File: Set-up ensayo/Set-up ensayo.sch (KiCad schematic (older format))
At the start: 0 parts

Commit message: Terminé con el paso 1 de proceso y comencé con el paso 2 colocando componentes, falta el interruptor para cambiar de estado del PCB (ensayo/configuración)
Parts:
- added H? (x4): MountingHole_Pad, symbol Mechanical:MountingHole_Pad
- added J?: Conn_Coaxial, symbol Connector:Conn_Coaxial
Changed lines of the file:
@@
 EESchema Schematic File Version 4
+LIBS:Set-up ensayo-cache
 EELAYER 29 0
 EELAYER END
@@
 Comment4 ""
 $EndDescr
+$Comp
+L Mechanical:MountingHole_Pad H?
+U 1 1 5D42DD18
+P 2650 2850
+F 0 "H?" H 2750 2899 50  0000 L CNN
+F 1 "MountingHole_Pad" H 2750 2808 50  0000 L CNN
+F 2 "" H 2650 2850 50  0001 C CNN
+F 3 "~" H 2650 2850 50  0001 C CNN
+	1    2650 2850
+	1    0    0    -1
+$EndComp
+$Comp
+L Mechanical:MountingHole_Pad H?
+U 1 1 5D42E2DA
+P 5150 2850
+F 0 "H?" H 5250 2899 50  0000 L CNN
+F 1 "MountingHole_Pad" H 5250 2808 50  0000 L CNN
+F 2 "" H 5150 2850 50  0001 C CNN
+F 3 "~" H 5150 2850 50  0001 C CNN
+	1    5150 2850
+	1    0    0    -1
+$EndComp
+$Comp
+L Mechanical:MountingHole_Pad H?
+U 1 1 5D42E927
+P 2650 5000
+F 0 "H?" H 2750 5049 50  0000 L CNN
+F 1 "MountingHole_Pad" H 2750 4958 50  0000 L CNN
+F 2 "" H 2650 5000 50  0001 C CNN
+F 3 "~" H 2650 5000 50  0001 C CNN
+	1    2650 5000
+	1    0    0    -1
+$EndComp
+$Comp
+L Mechanical:MountingHole_Pad H?
+U 1 1 5D42EA1B
+P 5200 5100
+F 0 "H?" H 5300 5149 50  0000 L CNN
+F 1 "MountingHole_Pad" H 5300 5058 50  0000 L CNN
+F 2 "" H 5200 5100 50  0001 C CNN
+F 3 "~" H 5200 5100 50  0001 C CNN
+	1    5200 5100
+	1    0    0    -1
+$EndComp
+$Comp
+L Connector:Conn_Coaxial J?
+U 1 1 5D42F04D
+P 3200 3800
+F 0 "J?" H 3300 3775 50  0000 L CNN
+F 1 "Conn_Coaxial" H 3300 3684 50  0000 L CNN
+F 2 "" H 3200 3800 50  0001 C CNN
+F 3 " ~" H 3200 3800 50  0001 C CNN
+	1    3200 3800
+	1    0    0    -1
+$EndComp
 $EndSCHEMATC

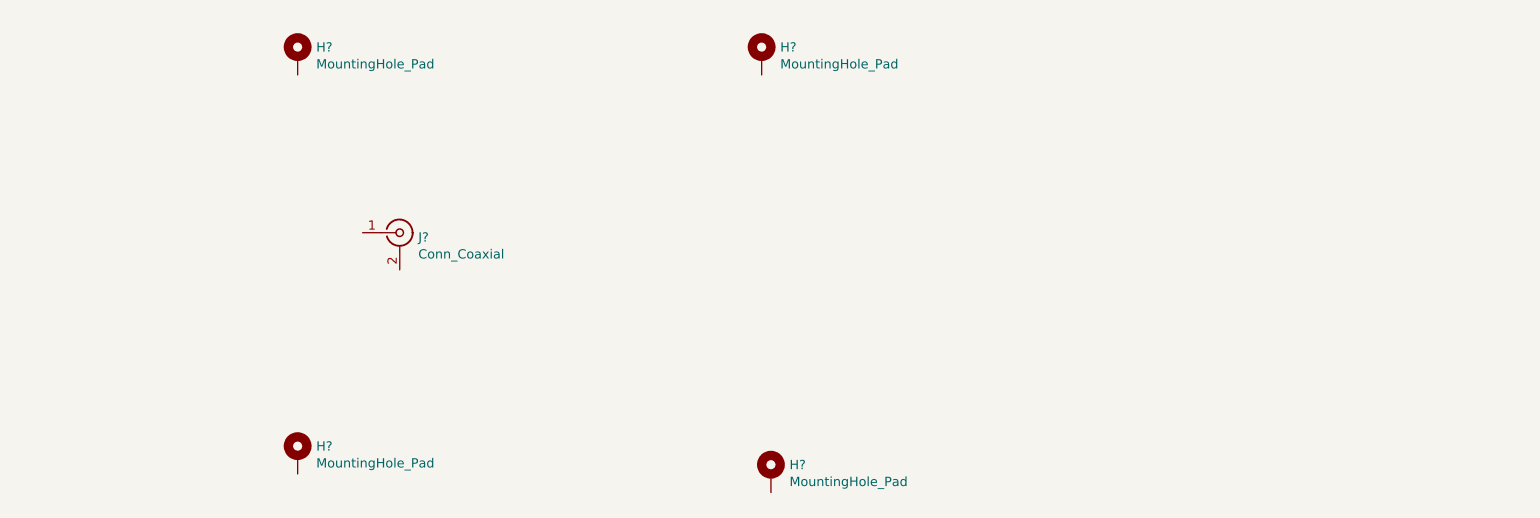
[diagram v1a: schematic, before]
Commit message: Cree componente circuit breaker en librería nueva Simbolo-ensayo y comencé a colocar los símbolos de los componentes
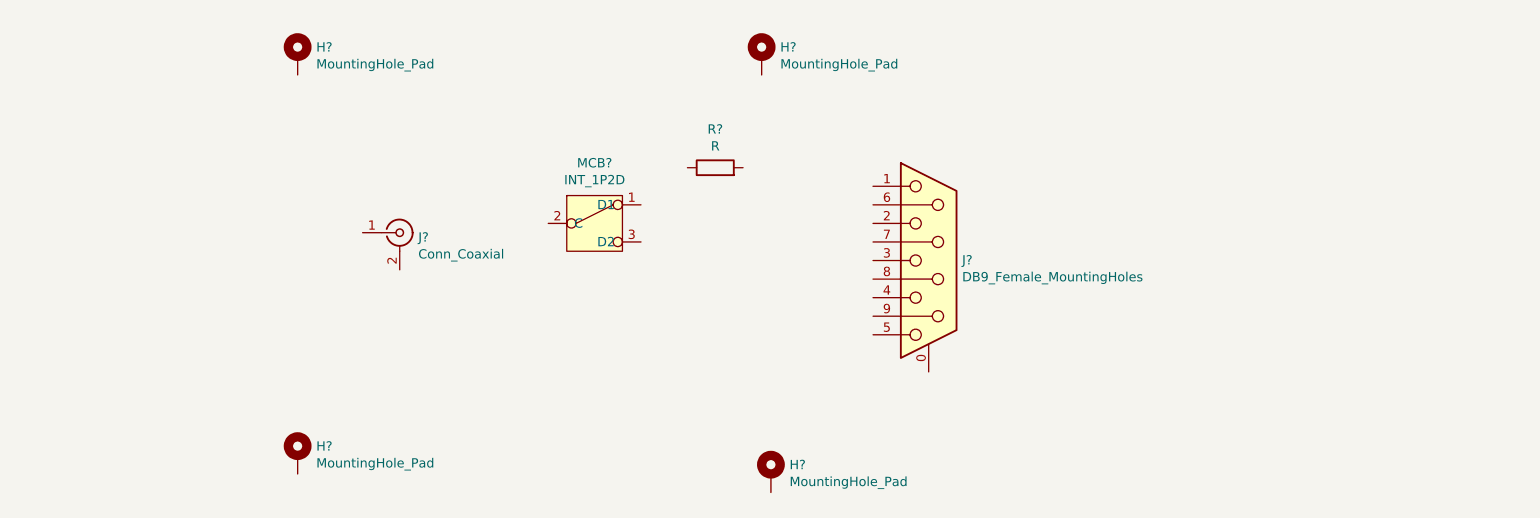
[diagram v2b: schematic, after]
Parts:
- added J?: DB9_Female_MountingHoles, symbol Connector:DB9_Female_MountingHoles
- added MCB?: INT_1P2D, symbol Simbolo-ensayo:INT_1P2D
- added R?: R, symbol Device:R
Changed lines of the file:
@@
+	1    0    0    -1
+$EndComp
+$Comp
+L Simbolo-ensayo:INT_1P2D MCB?
+U 1 1 5D440928
+P 4250 3750
+F 0 "MCB?" H 4250 4075 50  0000 C CNN
+F 1 "INT_1P2D" H 4250 3984 50  0000 C CNN
+F 2 "" H 4250 3750 50  0001 C CNN
+F 3 "" H 4250 3750 50  0001 C CNN
+	1    4250 3750
+	1    0    0    -1
+$EndComp
+$Comp
+L Device:R R?
+U 1 1 5D441970
+P 4900 3450
+F 0 "R?" V 5107 3450 50  0000 C CNN
+F 1 "R" V 5016 3450 50  0000 C CNN
+F 2 "" V 4830 3450 50  0001 C CNN
+F 3 "~" H 4900 3450 50  0001 C CNN
+	1    4900 3450
+	0    -1   -1   0
+$EndComp
+$Comp
+L Connector:DB9_Female_MountingHoles J?
+U 1 1 5D442DB3
+P 6050 3950
+F 0 "J?" H 6230 3952 50  0000 L CNN
+F 1 "DB9_Female_MountingHoles" H 6230 3861 50  0000 L CNN
+F 2 "" H 6050 3950 50  0001 C CNN
+F 3 " ~" H 6050 3950 50  0001 C CNN
+	1    6050 3950
 	1    0    0    -1
 $EndComp

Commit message: Agregué puntos de pruebas y campo de función en cada componente del esquema, fin de segundo paso en proceso
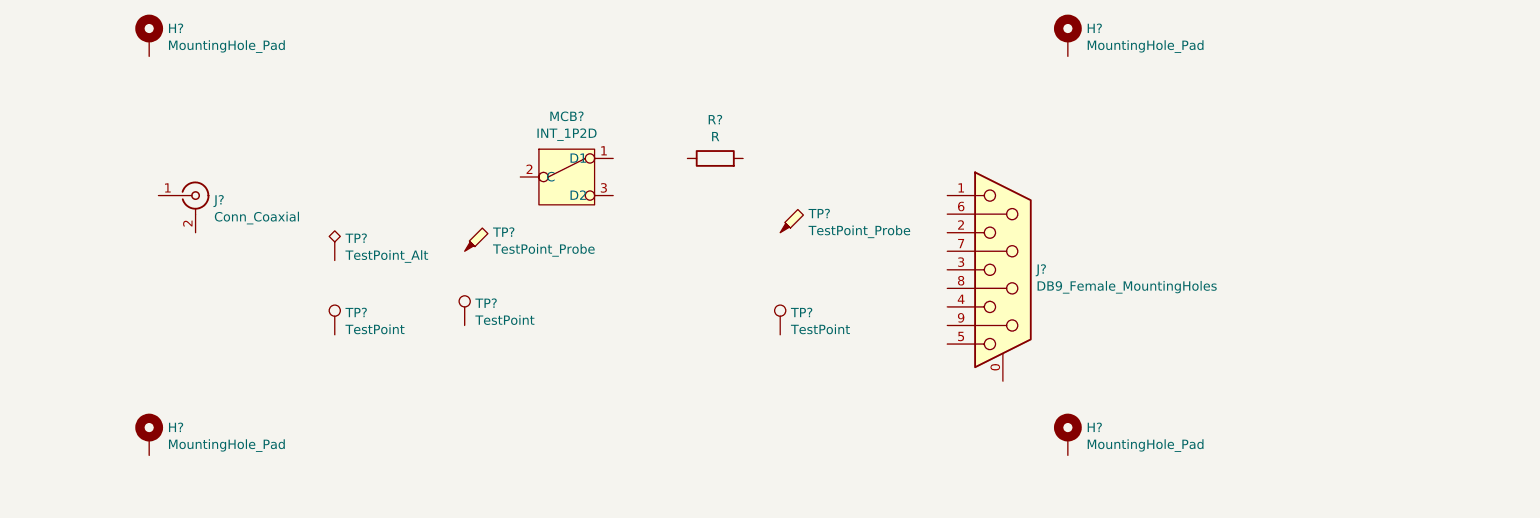
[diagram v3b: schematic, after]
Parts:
- added TP? (x2): TestPoint_Probe, symbol Connector:TestPoint_Probe
- added TP? (x3): TestPoint, symbol Connector:TestPoint
- added TP?: TestPoint_Alt, symbol Connector:TestPoint_Alt
- H? (x4): Función (none) -> Fijación e interfaz eléctrica con chasis
- J?: Función (none) -> Interfaz eléctrica con generador de señales
- J?: Función (none) -> Interfaz eléctrica con sensores
- MCB?: Función (none) -> Interruptor HMI para cambio enter ajuste y ensayo
- R?: Función (none) -> Resistencia de medición de sensor
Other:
- moved on the sheet: H?, J?, MCB?, R?
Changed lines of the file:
@@
 L Mechanical:MountingHole_Pad H?
 U 1 1 5D42DD18
-P 2650 2850
-F 0 "H?" H 2750 2899 50  0000 L CNN
-F 1 "MountingHole_Pad" H 2750 2808 50  0000 L CNN
-F 2 "" H 2650 2850 50  0001 C CNN
-F 3 "~" H 2650 2850 50  0001 C CNN
-	1    2650 2850
+P 1850 2750
+F 0 "H?" H 1950 2799 50  0000 L CNN
+F 1 "MountingHole_Pad" H 1950 2708 50  0000 L CNN
+F 2 "" H 1850 2750 50  0001 C CNN
+F 3 "~" H 1850 2750 50  0001 C CNN
+F 4 "Fijación e interfaz eléctrica con chasis" H 1850 2750 50  0001 C CNN "Función"
+	1    1850 2750
 	1    0    0    -1
 $EndComp
@@
 L Mechanical:MountingHole_Pad H?
 U 1 1 5D42E2DA
-P 5150 2850
-F 0 "H?" H 5250 2899 50  0000 L CNN
-F 1 "MountingHole_Pad" H 5250 2808 50  0000 L CNN
-F 2 "" H 5150 2850 50  0001 C CNN
-F 3 "~" H 5150 2850 50  0001 C CNN
-	1    5150 2850
+P 6800 2750
+F 0 "H?" H 6900 2799 50  0000 L CNN
+F 1 "MountingHole_Pad" H 6900 2708 50  0000 L CNN
+F 2 "" H 6800 2750 50  0001 C CNN
+F 3 "~" H 6800 2750 50  0001 C CNN
+F 4 "Fijación e interfaz eléctrica con chasis" H 6800 2750 50  0001 C CNN "Función"
+	1    6800 2750
 	1    0    0    -1
 $EndComp
@@
 L Mechanical:MountingHole_Pad H?
 U 1 1 5D42E927
-P 2650 5000
-F 0 "H?" H 2750 5049 50  0000 L CNN
-F 1 "MountingHole_Pad" H 2750 4958 50  0000 L CNN
-F 2 "" H 2650 5000 50  0001 C CNN
-F 3 "~" H 2650 5000 50  0001 C CNN
-	1    2650 5000
+P 1850 4900
+F 0 "H?" H 1950 4949 50  0000 L CNN
+F 1 "MountingHole_Pad" H 1950 4858 50  0000 L CNN
+F 2 "" H 1850 4900 50  0001 C CNN
+F 3 "~" H 1850 4900 50  0001 C CNN
+F 4 "Fijación e interfaz eléctrica con chasis" H 1850 4900 50  0001 C CNN "Función"
+	1    1850 4900
 	1    0    0    -1
 $EndComp
@@
 L Mechanical:MountingHole_Pad H?
 U 1 1 5D42EA1B
-P 5200 5100
-F 0 "H?" H 5300 5149 50  0000 L CNN
-F 1 "MountingHole_Pad" H 5300 5058 50  0000 L CNN
-F 2 "" H 5200 5100 50  0001 C CNN
-F 3 "~" H 5200 5100 50  0001 C CNN
-	1    5200 5100
+P 6800 4900
+F 0 "H?" H 6900 4949 50  0000 L CNN
+F 1 "MountingHole_Pad" H 6900 4858 50  0000 L CNN
+F 2 "" H 6800 4900 50  0001 C CNN
+F 3 "~" H 6800 4900 50  0001 C CNN
+F 4 "Fijación e interfaz eléctrica con chasis" H 6800 4900 50  0001 C CNN "Función"
+	1    6800 4900
 	1    0    0    -1
 $EndComp
@@
 L Connector:Conn_Coaxial J?
 U 1 1 5D42F04D
-P 3200 3800
-F 0 "J?" H 3300 3775 50  0000 L CNN
-F 1 "Conn_Coaxial" H 3300 3684 50  0000 L CNN
-F 2 "" H 3200 3800 50  0001 C CNN
-F 3 " ~" H 3200 3800 50  0001 C CNN
-	1    3200 3800
+P 2100 3600
+F 0 "J?" H 2200 3575 50  0000 L CNN
+F 1 "Conn_Coaxial" H 2200 3484 50  0000 L CNN
+F 2 "" H 2100 3600 50  0001 C CNN
+F 3 " ~" H 2100 3600 50  0001 C CNN
+F 4 "Interfaz eléctrica con generador de señales" H 2100 3600 50  0001 C CNN "Función"
+	1    2100 3600
 	1    0    0    -1
 $EndComp
@@
 L Simbolo-ensayo:INT_1P2D MCB?
 U 1 1 5D440928
-P 4250 3750
-F 0 "MCB?" H 4250 4075 50  0000 C CNN
-F 1 "INT_1P2D" H 4250 3984 50  0000 C CNN
-F 2 "" H 4250 3750 50  0001 C CNN
-F 3 "" H 4250 3750 50  0001 C CNN
-	1    4250 3750
+P 4100 3500
+F 0 "MCB?" H 4100 3825 50  0000 C CNN
+F 1 "INT_1P2D" H 4100 3734 50  0000 C CNN
+F 2 "" H 4100 3500 50  0001 C CNN
+F 3 "" H 4100 3500 50  0001 C CNN
+F 4 "Interruptor HMI para cambio enter ajuste y ensayo" H 4100 3500 50  0001 C CNN "Función"
+	1    4100 3500
 	1    0    0    -1
 $EndComp
@@
 L Device:R R?
 U 1 1 5D441970
-P 4900 3450
-F 0 "R?" V 5107 3450 50  0000 C CNN
-F 1 "R" V 5016 3450 50  0000 C CNN
-F 2 "" V 4830 3450 50  0001 C CNN
-F 3 "~" H 4900 3450 50  0001 C CNN
-	1    4900 3450
+P 4900 3400
+F 0 "R?" V 5107 3400 50  0000 C CNN
+F 1 "R" V 5016 3400 50  0000 C CNN
+F 2 "" V 4830 3400 50  0001 C CNN
+F 3 "~" H 4900 3400 50  0001 C CNN
+F 4 "Resistencia de medición de sensor" V 4900 3400 50  0001 C CNN "Función"
+	1    4900 3400
 	0    -1   -1   0
 $EndComp
@@
 L Connector:DB9_Female_MountingHoles J?
 U 1 1 5D442DB3
-P 6050 3950
-F 0 "J?" H 6230 3952 50  0000 L CNN
-F 1 "DB9_Female_MountingHoles" H 6230 3861 50  0000 L CNN
-F 2 "" H 6050 3950 50  0001 C CNN
-F 3 " ~" H 6050 3950 50  0001 C CNN
-	1    6050 3950
+P 6450 4000
+F 0 "J?" H 6630 4002 50  0000 L CNN
+F 1 "DB9_Female_MountingHoles" H 6630 3911 50  0000 L CNN
+F 2 "" H 6450 4000 50  0001 C CNN
+F 3 " ~" H 6450 4000 50  0001 C CNN
+F 4 "Interfaz eléctrica con sensores" H 6450 4000 50  0001 C CNN "Función"
+	1    6450 4000
 	1    0    0    -1
 $EndComp
+$Comp
+L Connector:TestPoint_Probe TP?
+U 1 1 5D483898
+P 3550 3900
+F 0 "TP?" H 3703 4001 50  0000 L CNN
+F 1 "TestPoint_Probe" H 3703 3910 50  0000 L CNN
+F 2 "" H 3750 3900 50  0001 C CNN
+F 3 "~" H 3750 3900 50  0001 C CNN
+F 4 "Interfaz eléctrica con punta de medición V1 osciloscopio" H 3550 3900 50  0001 C CNN "Función"
+	1    3550 3900
+	1    0    0    -1
+$EndComp
+$Comp
+L Connector:TestPoint_Probe TP?
+U 1 1 5D484196
+P 5250 3800
+F 0 "TP?" H 5403 3901 50  0000 L CNN
+F 1 "TestPoint_Probe" H 5403 3810 50  0000 L CNN
+F 2 "" H 5450 3800 50  0001 C CNN
+F 3 "~" H 5450 3800 50  0001 C CNN
+F 4 "Interfaz eléctrica con punta de medición V2 osciloscopio" H 5250 3800 50  0001 C CNN "Función"
+	1    5250 3800
+	1    0    0    -1
+$EndComp
+$Comp
+L Connector:TestPoint TP?
+U 1 1 5D4852D2
+P 5250 4350
+F 0 "TP?" H 5308 4468 50  0000 L CNN
+F 1 "TestPoint" H 5308 4377 50  0000 L CNN
+F 2 "" H 5450 4350 50  0001 C CNN
+F 3 "~" H 5450 4350 50  0001 C CNN
+F 4 "Interfaz eléctrica con GND de V2 osciloscopio" H 5250 4350 50  0001 C CNN "Función"
+	1    5250 4350
+	1    0    0    -1
+$EndComp
+$Comp
+L Connector:TestPoint TP?
+U 1 1 5D4861BC
+P 3550 4300
+F 0 "TP?" H 3608 4418 50  0000 L CNN
+F 1 "TestPoint" H 3608 4327 50  0000 L CNN
+F 2 "" H 3750 4300 50  0001 C CNN
+F 3 "~" H 3750 4300 50  0001 C CNN
+F 4 "Interfaz eléctrica con GND de V1 osciloscopio" H 3550 4300 50  0001 C CNN "Función"
+	1    3550 4300
+	1    0    0    -1
+$EndComp
+$Comp
+L Connector:TestPoint_Alt TP?
+U 1 1 5D486AED
+P 2850 3950
+F 0 "TP?" H 2908 4068 50  0000 L CNN
+F 1 "TestPoint_Alt" H 2908 3977 50  0000 L CNN
+F 2 "" H 3050 3950 50  0001 C CNN
+F 3 "~" H 3050 3950 50  0001 C CNN
+F 4 "Interfaz eléctrica con potencial positivo tester" H 2850 3950 50  0001 C CNN "Función"
+	1    2850 3950
+	1    0    0    -1
+$EndComp
+$Comp
+L Connector:TestPoint TP?
+U 1 1 5D487102
+P 2850 4350
+F 0 "TP?" H 2908 4468 50  0000 L CNN
+F 1 "TestPoint" H 2908 4377 50  0000 L CNN
+F 2 "" H 3050 4350 50  0001 C CNN
+F 3 "~" H 3050 4350 50  0001 C CNN
+F 4 "Interfaz eléctrica con potencial negativo tester" H 2850 4350 50  0001 C CNN "Función"
+	1    2850 4350
+	1    0    0    -1
+$EndComp

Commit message: Paso 3 de proceso de diseño, agrupé a los componentes por función y les puse designador. Queda pendiente asociar a footprints pero debo contar con un calibre para verificarlos
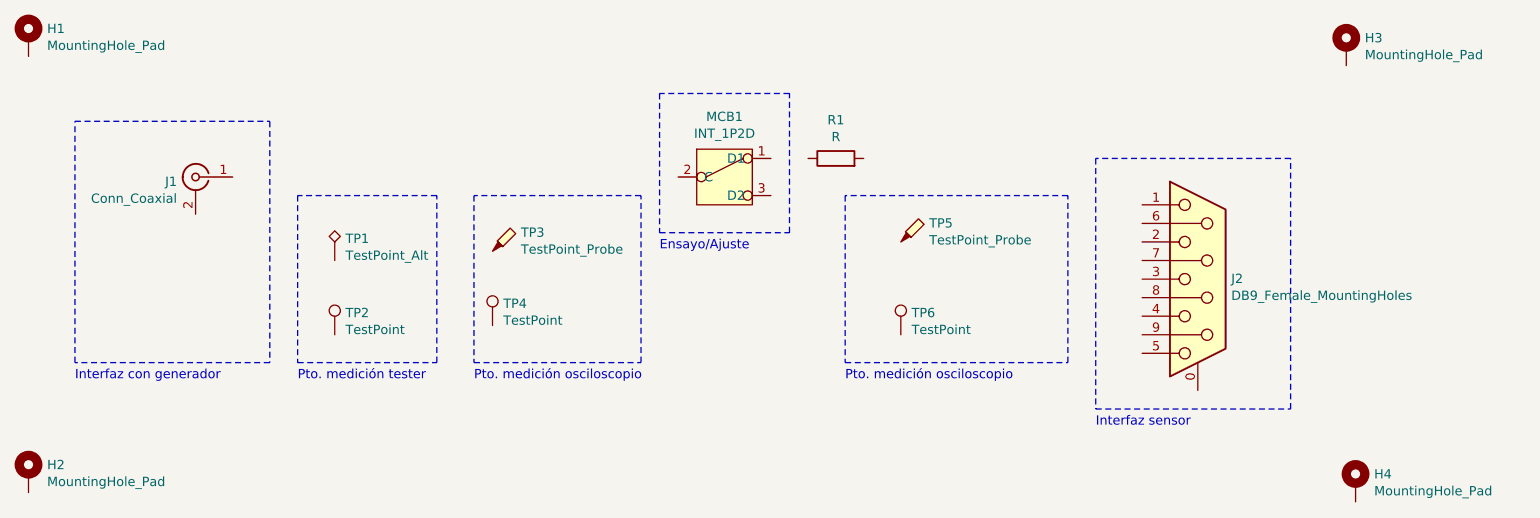
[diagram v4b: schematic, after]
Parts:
- gave numbers to parts that had none: 14
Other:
- note added: "Ensayo/Ajuste"
- note added: "Interfaz con generador"
- note added: "Interfaz sensor"
- note added: "Pto. medición osciloscopio"
- note added: "Pto. medición tester"
- moved on the sheet: H1, H2, H3, H4, J1, J2, MCB1, R1, TP3, TP4, TP5, TP6
